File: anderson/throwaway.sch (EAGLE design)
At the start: 5 parts

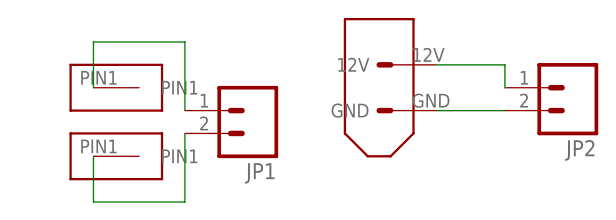
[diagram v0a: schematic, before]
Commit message: Anderson Throwaways
25 Amp Andersons on throwaway boards with XT60 connectors.
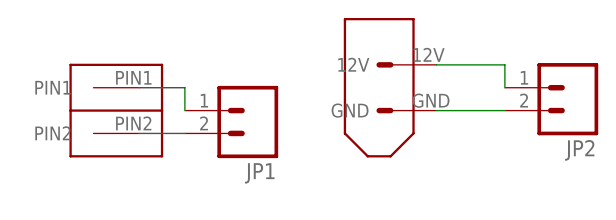
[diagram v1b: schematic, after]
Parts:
- removed U$2: ANDERSON_RA_BOTTOM, pie:ANDERSON_RA_BOTTOM
- U$1: value ANDERSON_RA_BOTTOM -> ANDERSON_25A_1X2; device pie:ANDERSON_RA_BOTTOM -> pie:ANDERSON_25A_1X2
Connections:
- net N$2: now also U$1.PIN2; no longer U$2.PIN1
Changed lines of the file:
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@@
 <part name="U$3" library="pie" deviceset="XT60CONNECTOR" device=""/>
 <part name="JP2" library="pie" deviceset="M02" device="1X02-MTA"/>
-<part name="U$1" library="pie" deviceset="ANDERSON_RA_BOTTOM" device=""/>
-<part name="U$2" library="pie" deviceset="ANDERSON_RA_BOTTOM" device=""/>
+<part name="U$1" library="pie" deviceset="ANDERSON_25A_1X2" device=""/>
 </parts>
 <sheets>
@@
 <instance part="U$3" gate="G$1" x="38.1" y="17.78" rot="R270"/>
 <instance part="JP2" gate="G$1" x="60.96" y="17.78" rot="R180"/>
-<instance part="U$1" gate="G$1" x="7.62" y="17.78"/>
-<instance part="U$2" gate="G$1" x="7.62" y="10.16"/>
+<instance part="U$1" gate="G$1" x="5.08" y="20.32" rot="R270"/>
 </instances>
 <busses>
@@
 <segment>
 <pinref part="U$1" gate="G$1" pin="PIN1"/>
-<wire x1="7.62" y1="17.78" x2="7.62" y2="22.86" width="0.1524" layer="91"/>
 <pinref part="JP1" gate="G$1" pin="1"/>
-<wire x1="7.62" y1="22.86" x2="17.78" y2="22.86" width="0.1524" layer="91"/>
-<wire x1="17.78" y1="22.86" x2="17.78" y2="15.24" width="0.1524" layer="91"/>
+<wire x1="12.7" y1="17.78" x2="17.78" y2="17.78" width="0.1524" layer="91"/>
+<wire x1="17.78" y1="17.78" x2="17.78" y2="15.24" width="0.1524" layer="91"/>
 </segment>
 </net>
 <net name="N$2" class="0">
 <segment>
-<pinref part="U$2" gate="G$1" pin="PIN1"/>
-<wire x1="7.62" y1="10.16" x2="7.62" y2="5.08" width="0.1524" layer="91"/>
+<pinref part="U$1" gate="G$1" pin="PIN2"/>
 <pinref part="JP1" gate="G$1" pin="2"/>
-<wire x1="7.62" y1="5.08" x2="17.78" y2="5.08" width="0.1524" layer="91"/>
-<wire x1="17.78" y1="5.08" x2="17.78" y2="12.7" width="0.1524" layer="91"/>
+<wire x1="12.7" y1="12.7" x2="17.78" y2="12.7" width="0.1524" layer="91"/>
 </segment>
 </net>

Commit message: Anderson Throwaway
Replaced wrong anderson on throwaway with correct 25A andersons
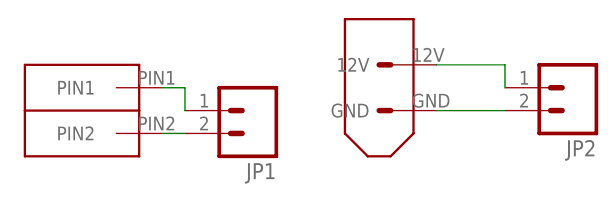
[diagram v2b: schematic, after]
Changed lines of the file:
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@@
 <instance part="U$3" gate="G$1" x="38.1" y="17.78" rot="R270"/>
 <instance part="JP2" gate="G$1" x="60.96" y="17.78" rot="R180"/>
-<instance part="U$1" gate="G$1" x="5.08" y="20.32" rot="R270"/>
+<instance part="U$1" gate="G$1" x="0" y="20.32" rot="R270"/>
 </instances>
 <busses>
@@
 <net name="N$1" class="0">
 <segment>
+<pinref part="JP1" gate="G$1" pin="1"/>
+<wire x1="17.78" y1="17.78" x2="17.78" y2="15.24" width="0.1524" layer="91"/>
 <pinref part="U$1" gate="G$1" pin="PIN1"/>
-<pinref part="JP1" gate="G$1" pin="1"/>
-<wire x1="12.7" y1="17.78" x2="17.78" y2="17.78" width="0.1524" layer="91"/>
-<wire x1="17.78" y1="17.78" x2="17.78" y2="15.24" width="0.1524" layer="91"/>
+<wire x1="15.24" y1="17.78" x2="17.78" y2="17.78" width="0.1524" layer="91"/>
 </segment>
 </net>
@@
 <pinref part="U$1" gate="G$1" pin="PIN2"/>
 <pinref part="JP1" gate="G$1" pin="2"/>
-<wire x1="12.7" y1="12.7" x2="17.78" y2="12.7" width="0.1524" layer="91"/>
+<wire x1="15.24" y1="12.7" x2="17.78" y2="12.7" width="0.1524" layer="91"/>
 </segment>
 </net>

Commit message: Throwaway Board
XT60 Connectors and Anderson Connnectors  on throwaway
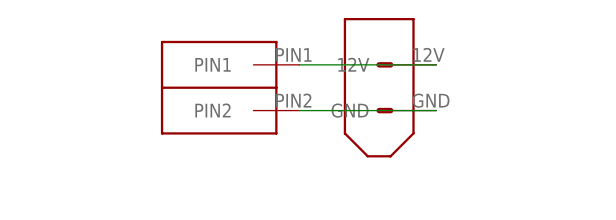
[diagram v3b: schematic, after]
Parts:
- removed JP1, JP2: (no value), pie:M021X02-MTA
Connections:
- removed net N$3: JP2.2, U$3.GND
- removed net N$4: JP2.1, U$3.12V
- net N$1: now also U$3.12V; no longer JP1.1
- net N$2: now also U$3.GND; no longer JP1.2
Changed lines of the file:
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@@
 </classes>
 <parts>
-<part name="JP1" library="pie" deviceset="M02" device="1X02-MTA"/>
 <part name="U$3" library="pie" deviceset="XT60CONNECTOR" device=""/>
-<part name="JP2" library="pie" deviceset="M02" device="1X02-MTA"/>
 <part name="U$1" library="pie" deviceset="ANDERSON_25A_1X2" device=""/>
 </parts>
@@
 </plain>
 <instances>
-<instance part="JP1" gate="G$1" x="25.4" y="15.24" rot="R180"/>
 <instance part="U$3" gate="G$1" x="38.1" y="17.78" rot="R270"/>
-<instance part="JP2" gate="G$1" x="60.96" y="17.78" rot="R180"/>
-<instance part="U$1" gate="G$1" x="0" y="20.32" rot="R270"/>
+<instance part="U$1" gate="G$1" x="15.24" y="22.86" rot="R270"/>
 </instances>
 <busses>
 </busses>
 <nets>
-<net name="N$3" class="0">
-<segment>
-<pinref part="U$3" gate="G$1" pin="GND"/>
-<pinref part="JP2" gate="G$1" pin="2"/>
-<wire x1="45.72" y1="15.24" x2="53.34" y2="15.24" width="0.1524" layer="91"/>
-</segment>
-</net>
-<net name="N$4" class="0">
+<net name="N$1" class="0">
 <segment>
 <pinref part="U$3" gate="G$1" pin="12V"/>
-<pinref part="JP2" gate="G$1" pin="1"/>
-<wire x1="45.72" y1="20.32" x2="53.34" y2="20.32" width="0.1524" layer="91"/>
-<wire x1="53.34" y1="20.32" x2="53.34" y2="17.78" width="0.1524" layer="91"/>
-</segment>
-</net>
-<net name="N$1" class="0">
-<segment>
-<pinref part="JP1" gate="G$1" pin="1"/>
-<wire x1="17.78" y1="17.78" x2="17.78" y2="15.24" width="0.1524" layer="91"/>
 <pinref part="U$1" gate="G$1" pin="PIN1"/>
-<wire x1="15.24" y1="17.78" x2="17.78" y2="17.78" width="0.1524" layer="91"/>
+<wire x1="30.48" y1="20.32" x2="45.72" y2="20.32" width="0.1524" layer="91"/>
 </segment>
 </net>
 <net name="N$2" class="0">
 <segment>
+<pinref part="U$3" gate="G$1" pin="GND"/>
 <pinref part="U$1" gate="G$1" pin="PIN2"/>
-<pinref part="JP1" gate="G$1" pin="2"/>
-<wire x1="15.24" y1="12.7" x2="17.78" y2="12.7" width="0.1524" layer="91"/>
+<wire x1="30.48" y1="15.24" x2="45.72" y2="15.24" width="0.1524" layer="91"/>
 </segment>
 </net>

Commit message: Throwaway Board again...
removed traces used polygon instead.
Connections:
- net N$1 renamed 1
- net N$2 renamed 2
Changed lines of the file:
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@@
 </busses>
 <nets>
-<net name="N$1" class="0">
+<net name="1" class="0">
 <segment>
 <pinref part="U$3" gate="G$1" pin="12V"/>
@@
 </segment>
 </net>
-<net name="N$2" class="0">
+<net name="2" class="0">
 <segment>
 <pinref part="U$3" gate="G$1" pin="GND"/>
